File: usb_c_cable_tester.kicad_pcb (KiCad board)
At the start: 2 copper layers, 85.6 x 54 mm, 60 parts, among them J1 USB_C_Receptacle, J2 USB_C_Receptacle_ALLPINS, J3 USB_B_Micro, J4 USB3_B, J5 USB_B_Mini, J6 USB3_A

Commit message: Moved from https://github.com/SmittyHalibut/usb_c_cable_tester/tree/v2.2-jlcpcb #32
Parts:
- removed REF**: TestPoint_Plated_Hole_D5.0mm, TestPoint:TestPoint_Plated_Hole_D5.0mm
- removed REF**: OSHW-Logo_11.4x12mm_SilkScreen, Symbol:OSHW-Logo_11.4x12mm_SilkScreen
- J1: value USB_C_Receptacle -> USB C; footprint easyeda:USB-C-SMD_UT11113-11602-7H -> Libraries:USB_C_Receptacle_24P_QCHT_C456013
- J2: value USB_C_Receptacle_ALLPINS -> USB C; footprint easyeda:USB-C-SMD_UT11113-11602-7H -> Libraries:USB_C_Receptacle_24P_QCHT_C456013
- moved J1 3.32 mm to (140.0, 107.0)
- moved J2 3.05 mm to (60.3, 109.0)
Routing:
- net /SHLD: track 64.7 -> 61.8 mm
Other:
- board text added: "v2.2b"
- board text removed: "v2.2"

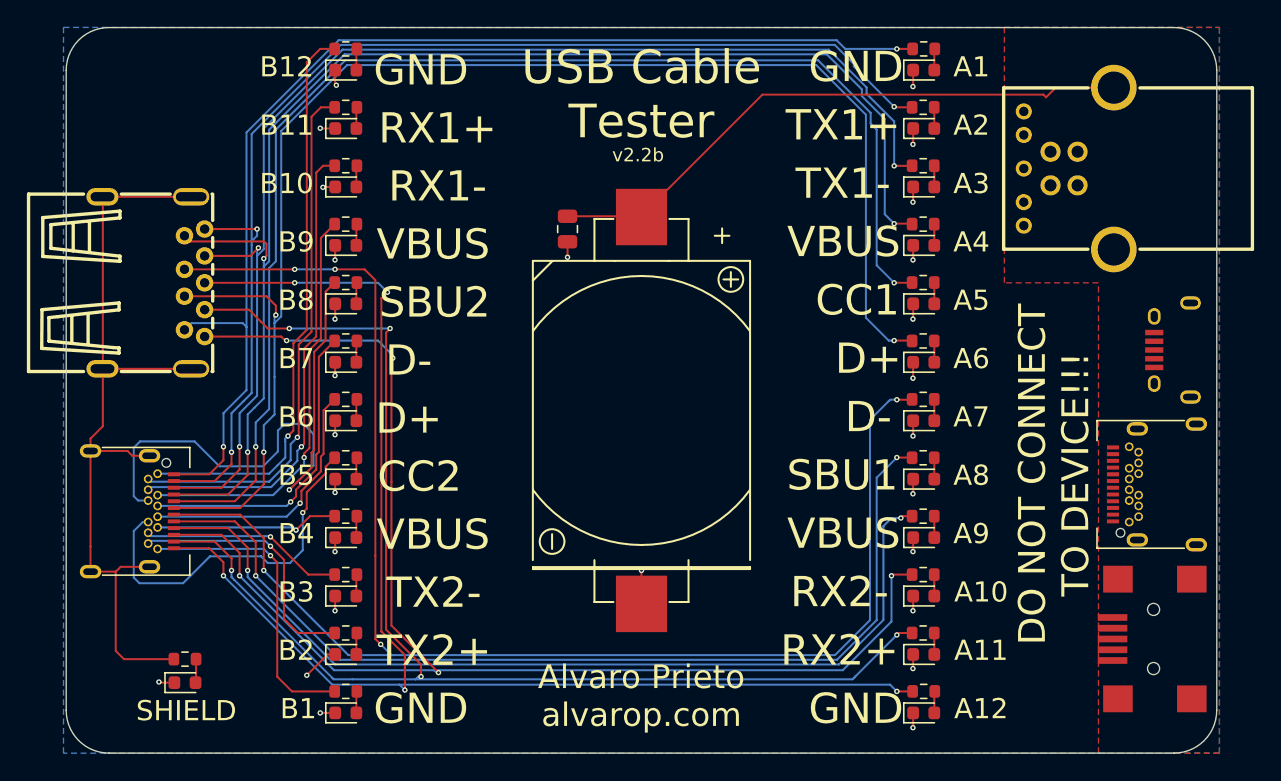
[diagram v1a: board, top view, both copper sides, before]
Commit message: v3.0. Vertical connectors, through hole where possible. #8, #19, #21, #36
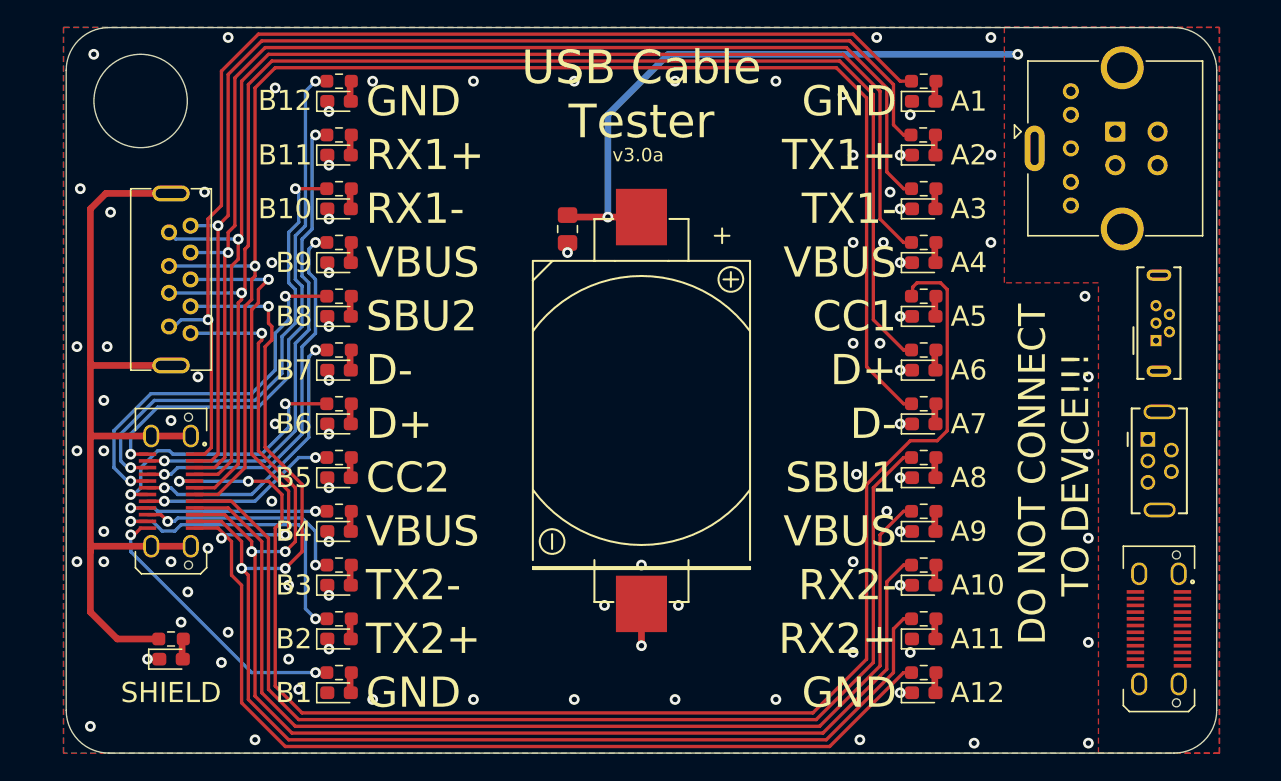
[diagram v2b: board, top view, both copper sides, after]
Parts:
- C1: footprint Capacitor_SMD:C_0805_2012Metric -> Capacitor_SMD:C_0805_2012Metric_Pad1.18x1.45mm_HandSolder
- D1, D10, D11, D12, D13, D14, D15, D16, D17, D18, D19, D2, D20, D21, D22, D23, D24, D25, D3, D4, D5, D6, D7, D8, D9: footprint LED_SMD:LED_0603_1608Metric -> LED_SMD:LED_0603_1608Metric_Pad1.05x0.95mm_HandSolder
- J1, J2: footprint Libraries:USB_C_Receptacle_24P_QCHT_C456013 -> Connector_USB:USB_C_Receptacle_JAE_DX07S024WJ3R400
- J3: footprint easyeda:MICRO-USB-SMD_10118194-0001LF -> Connector_USB:USB_Micro-B_Wuerth_614105150721_Vertical
- J4: footprint easyeda:USB-B-TH_XUNPU_USB-306BWD-ARW -> Libraries:USB_B_3.0_C2763106
- J5: footprint easyeda:MINI-USB-SMD_MINI-5PTP -> Connector_USB:USB_Mini-B_Tensility_54-00023_Vertical
- J6: footprint easyeda:USB-A-TH_U231-091N-5 -> Libraries:USB_A_3.0_HC-USB3.0-L137-ZP_C19273972
- R1, R10, R11, R12, R13, R14, R15, R16, R17, R18, R19, R2, R20, R21, R22, R23, R24, R25, R3, R4, R5, R6, R7, R8, R9: value 1k -> 2.2k; footprint Resistor_SMD:R_0603_1608Metric -> Resistor_SMD:R_0603_1608Metric_Pad0.98x0.95mm_HandSolder
- moved J5 14.9 mm to (137.7, 103.7), turned to -90 degrees
- moved J1 10.9 mm to (138.5, 117.8), turned to -90 degrees
- moved J2 4.94 mm to (65.0, 107.5)
- moved J4 3.77 mm to (135.2, 82.0)
- moved R25 2.45 mm to (77.5, 77.0)
- moved R22 2.40 mm to (121.0, 77.0)
- moved D25 2.38 mm to (77.5, 78.5)
- moved D22 2.33 mm to (121.0, 78.5)
- moved R9 2.11 mm to (77.5, 81.0)
- moved R7 2.05 mm to (121.0, 81.0)
- moved D9 2.04 mm to (77.5, 82.5)
- moved D21 2.03 mm to (65.0, 120.0)
- moved D7 1.98 mm to (121.0, 82.5)
- moved R21 1.82 mm to (65.0, 118.5)
- moved R10 1.78 mm to (77.5, 85.0)
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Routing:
- net GND: track 32.9 -> 3.11 mm, vias 27 -> 92
- net /SBU2: track 43.4 -> 28.7 mm, vias 1 -> 2
- net /CC2: track 26.9 -> 14.8 mm, vias 1 -> 2
- net /VBUS_A9: track 69.1 -> 79.1 mm, vias 2 -> 0
- net /SBU1: track 73.1 -> 82.4 mm, vias 2 -> 0
- net /D-_A: track 120.3 -> 111.2 mm, vias 5 -> 1
- net /CC1: track 96.2 -> 104.9 mm
- net /GND_A12: track 104.9 -> 100.4 mm, vias 5 -> 3
- net /RX2-: track 105.1 -> 101.3 mm, vias 5 -> 3
- net /RX1+: track 39.6 -> 35.9 mm, vias 1 -> 2
- net /TX2+: track 19.4 -> 22.7 mm, vias 1 -> 2
- net /VBUS_B4: track 13.7 -> 16.0 mm, vias 1 -> 2
- net /GND_B1: track 22.5 -> 20.4 mm, vias 1 -> 2
- net /D+_A: track 109.0 -> 106.8 mm, vias 3 -> 1
- net /GND_B12: track 42.5 -> 40.4 mm, vias 1 -> 2
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- added copper zone on F.Cu, net GND
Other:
- outline, holes or cut-outs redrawn
- board text added: "<><"
- board text added: "><>"
- board text added: "O"
- board text added: "Original design by Alvaro Prieto: alvarop.com v3.0 design by Mark Smith: halibut.com"
- board text added: "o"
- board text added: "v3.0a"
- board text removed: "Alvaro Prieto alvarop.com"
- board text removed: "v2.2b"
